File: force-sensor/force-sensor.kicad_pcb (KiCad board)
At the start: 2 copper layers, 50 x 20 mm, 32 parts, among them J101 Sensor Bridge, J103 PA2, J104 UPDI, J105 Supply, J106 Bus, U101 ATtiny416-M, U102 INA128, U103 ST3485, U201 TL431DBZ, U202 TPS560430Y

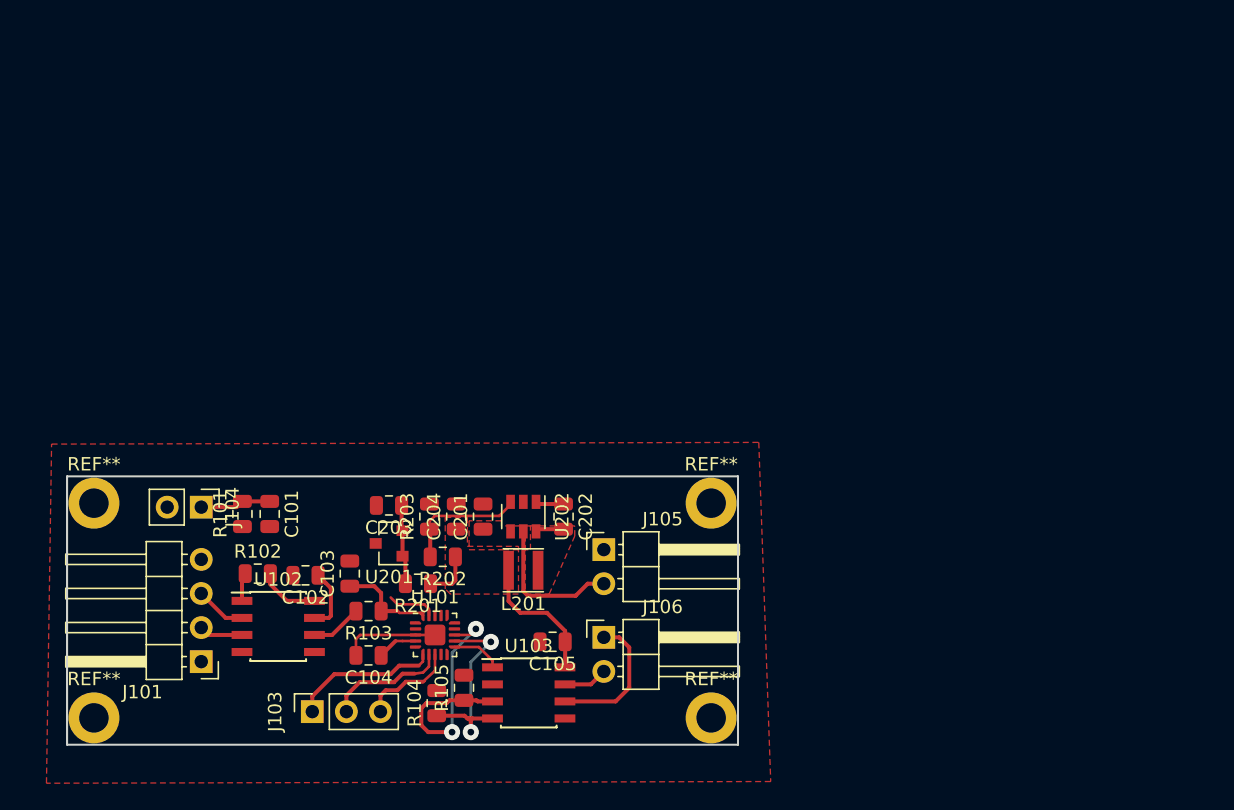
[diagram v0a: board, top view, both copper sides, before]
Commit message: Battry Protection added
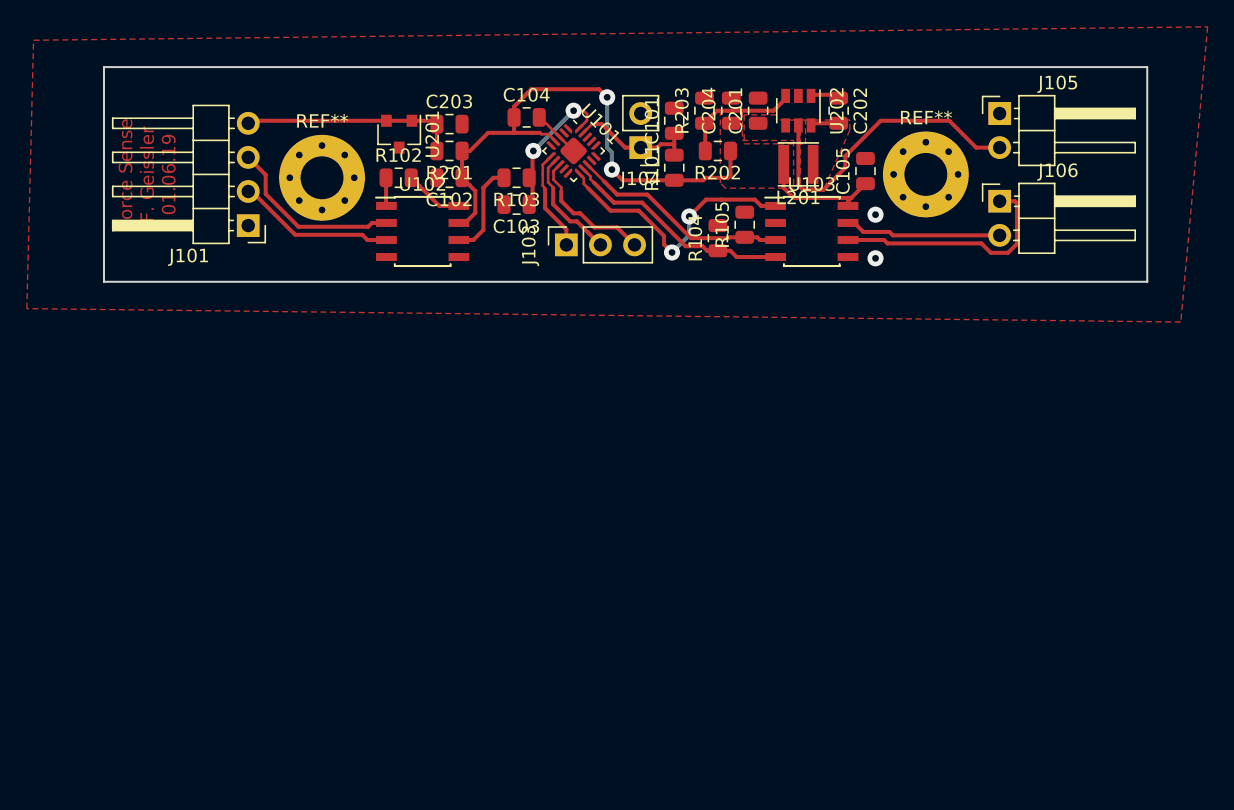
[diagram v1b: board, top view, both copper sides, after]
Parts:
- removed the REF** at (198.0, 82.0)
- removed the REF** at (198.0, 98.0)
- removed the REF** at (152.0, 98.0)
- removed the REF** at (152.0, 82.0)
- added REF**: MountingHole_3.2mm_M3_Pad_Via, MountingHole:MountingHole_3.2mm_M3_Pad_Via, F.Cu at (169.0, 57.8)
- added REF**: MountingHole_3.2mm_M3_Pad_Via, MountingHole:MountingHole_3.2mm_M3_Pad_Via, F.Cu at (214.0, 57.5)
- moved J105 43.9 mm to (219.5, 53.0)
- moved J106 43.9 mm to (219.5, 59.5)
- moved J104 42.3 mm to (192.8, 55.5), turned to 180 degrees
- moved C105 42.1 mm to (209.5, 57.2), turned to 90 degrees
- moved C101 42.0 mm to (195.2, 53.5), turned to 90 degrees
- moved C104 41.8 mm to (184.2, 53.2), turned to 0 degrees
- moved R101 41.2 mm to (195.2, 57.0)
- moved R104 40.5 mm to (198.5, 62.2)
- moved R105 40.4 mm to (200.5, 61.2)
- moved U103 40.3 mm to (205.5, 61.8)
- moved J103 39.6 mm to (187.2, 62.8)
- moved U101 37.5 mm to (187.8, 55.8), turned to 315 degrees
- moved C201 36.5 mm to (201.5, 52.8)
- moved C202 36.5 mm to (207.5, 52.8)
- moved C204 36.5 mm to (199.5, 52.8)
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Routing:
- net +3V3: track 21.6 -> 50.0 mm, vias 0 -> 2
- net /RXD: track 3.75 -> 20.4 mm, vias 0 -> 2
- net +12V: track 11.0 -> 23.1 mm
- net +2V5: track 5.95 -> 16.2 mm
- net Net-(J101-Pad3): track 3.79 -> 13.4 mm
- net Net-(J101-Pad2): track 3.26 -> 11.8 mm
- net Net-(J106-Pad2): track 3.30 -> 11.7 mm
- net Net-(J106-Pad1): track 10.4 -> 17.7 mm
- net GND: track 7.24 -> 3.60 mm, vias 0 -> 2
- net /VF: track 7.14 -> 10.7 mm, vias 0 -> 2
- net Net-(R103-Pad2): track 3.83 -> 7.13 mm
- net Net-(J103-Pad1): track 11.0 -> 7.72 mm
- net /TX_EN: track 19.6 -> 16.4 mm, vias 2 -> 0
- net Net-(J103-Pad3): track 7.37 -> 9.96 mm
- net /TXD: track 15.6 -> 17.2 mm, vias 2 -> 0
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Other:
- board size 50 x 20 mm -> 77.8 x 16 mm
- net class Default: clearance 0.2 -> 0.3
- rule trace_clearance: 0.2 -> 0.3
- board text added: "Force Sense F. Geissler 01.06.19"
